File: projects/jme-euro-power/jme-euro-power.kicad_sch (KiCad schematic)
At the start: 31 parts, among them J1 12V AC, J2 Eurorack 16 pin male power co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, U1 LM7812T, U2 LM7912

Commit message: Incremental checkin of schematic
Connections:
- net GND: now also J2.10 (GND), J2.12 (GND), J2.14 (-12V)
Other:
- moved on the sheet: C1, C10, C2, C3, C4, C5, C6, C7, C8, C9, D1, D2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

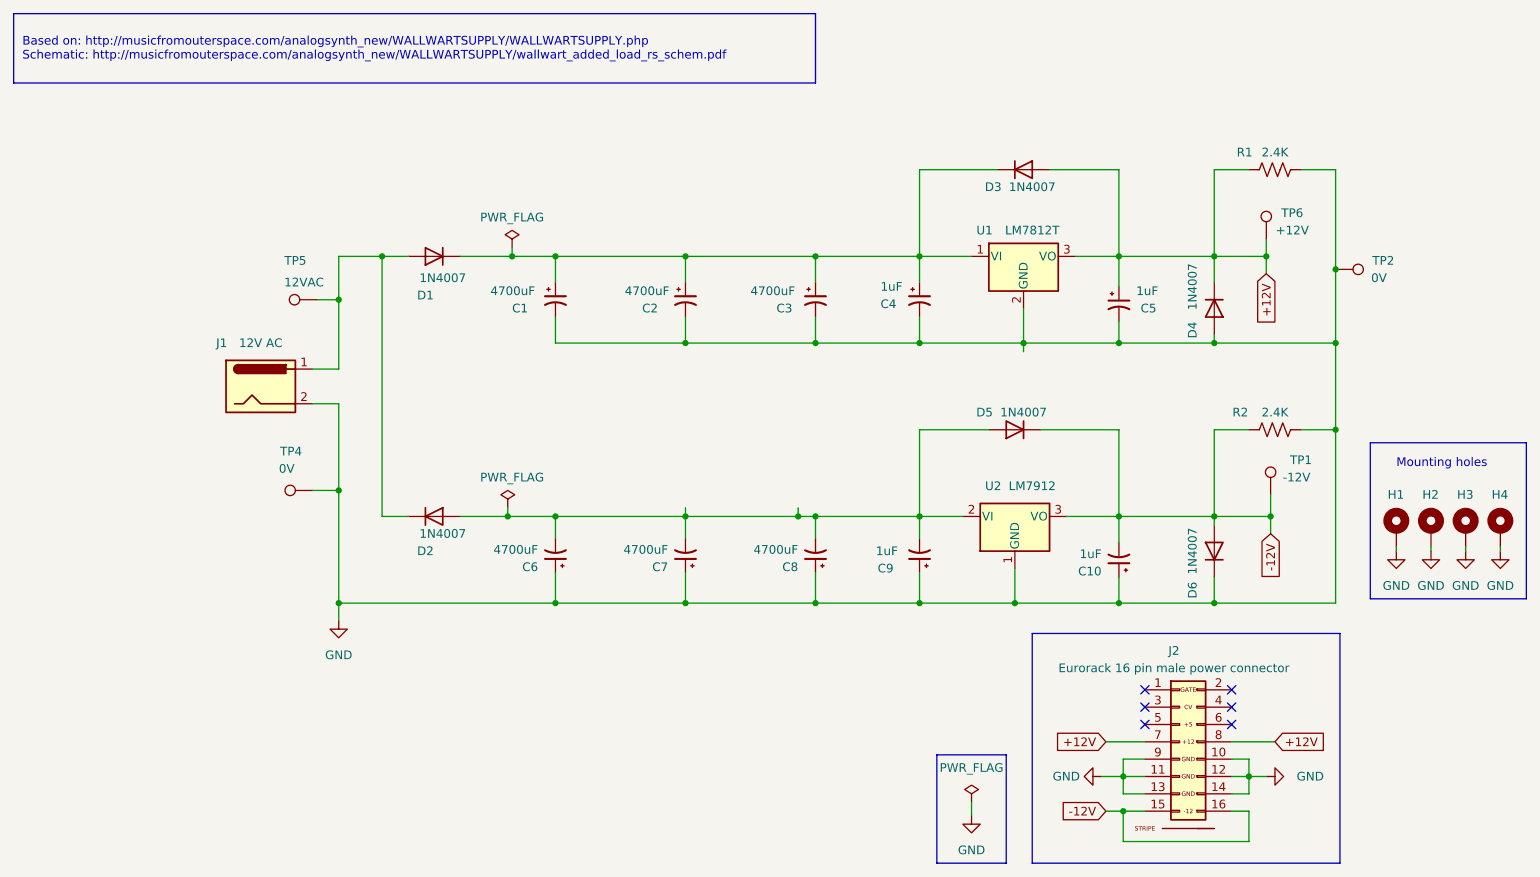
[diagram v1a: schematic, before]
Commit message: Completed PCB optimized for stripboard. All warnings resolved.
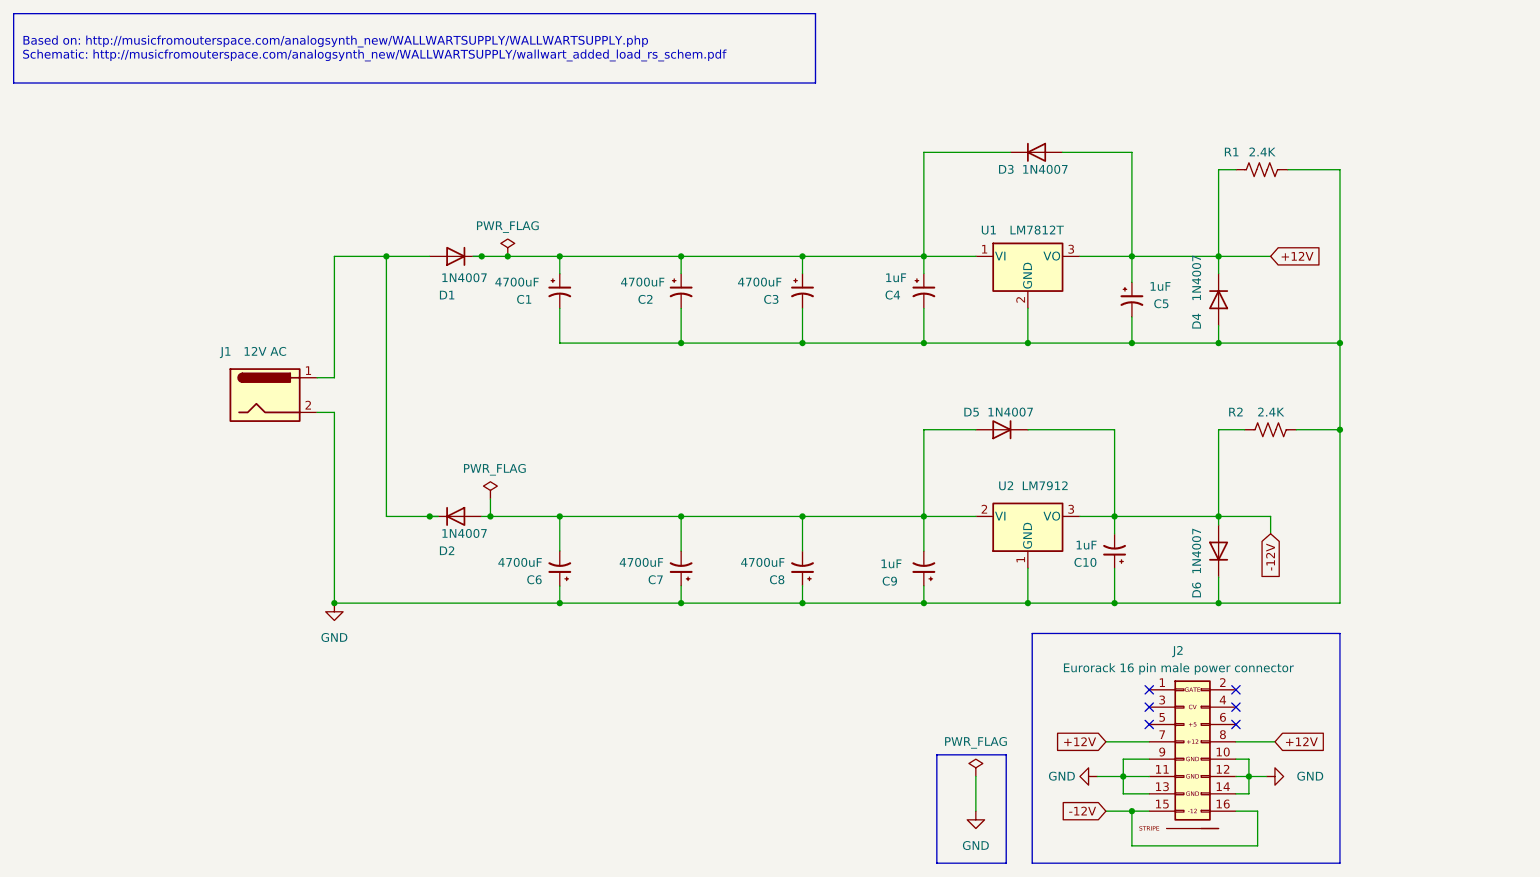
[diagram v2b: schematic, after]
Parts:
- removed H1, H2, H3, H4: MountingHole_Pad, MountingHole:MountingHole_3.2mm_M3_DIN965_Pad, symbol Mechanical:MountingHole_Pad
- removed TP1: -12V, 4ms_TestPoint:TestPoint_Pad_04, symbol Connector:TestPoint
- removed TP2, TP4: 0V, 4ms_TestPoint:TestPoint_Pad_04, symbol Connector:TestPoint
- removed TP5: 12VAC, 4ms_TestPoint:TestPoint_Pad_04, symbol Connector:TestPoint
- removed TP6: +12V, 4ms_TestPoint:TestPoint_Pad_04, symbol Connector:TestPoint
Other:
- note removed: "Mounting holes"
- moved on the sheet: C1, C10, C2, C3, C4, C5, C6, C7, C8, C9, D1, D2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
